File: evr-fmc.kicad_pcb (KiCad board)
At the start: 6 copper layers, 84 x 69 mm, 256 parts, among them J1 MMCX, J10 MMCX, J11 MMCX, J12 MMCX, J13 MMCX, J14 MMCX, J15 MMCX, J16 MMCX, J17 MMCX, J18 MMCX, J19 WP Jumper, J2 MMCX, J20 MMCX, J21 MMCX, J3 MMCX, J4 MMCX, J5 MMCX, J6 MMCX, J7 MMCX, J8 MMCX, J9 MMCX, P1 ASP-134488-01, Q1 FDN335N, Q2 FDN335N, Q3 FDN335N, T1 TCM2-43X+, T2 TCM2-43X+, T3 TCM2-43X+, T4 TCM2-43X+, U1 SN74LVC3G34DCT, U10 SN74LVC3G34DCT, U11 SN74LVC3G34DCT, U12 SN74LVC3G34DCT, U13 SN74LVC3G34DCT, U14 SN74LVC3G34DCT, U15 SN74LVC3G34DCT, U16 SN74LVC3G34DCT, U17 SN74LVC3G34DCT, U18 SI5394, U19 SI5394, U2 SN74LVC3G34DCT, U20 TLV75733PDBV, U21 TLV75718PDBV, U22 TPS562200, U23 74AVC4T245, U24 TLV75733PDBV, U25 74AVC4T245, U26 74LVC8T245, U27 74LVC8T245, U28 TLV75718PDBV, U3 SN74LVC3G34DCT, U4 SN74LVC3G34DCT, U5 SN74LVC3G34DCT, U6 SN74LVC3G34DCT, U7 SN74LVC3G34DCT, U8 SN74LVC3G34DCT, U9 AT24C64D, Y1 CX3225SB48000D0FPJC1, Y2 CX3225SB48000D0FPJC1

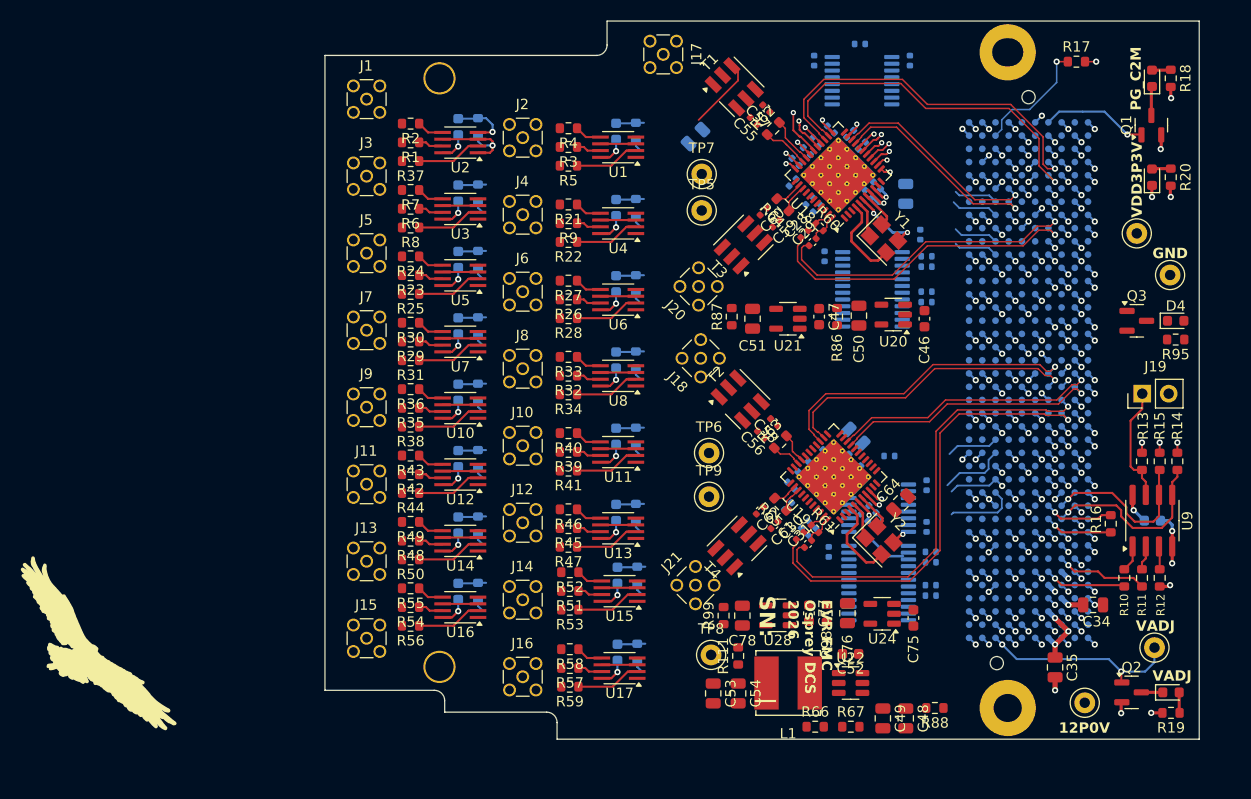
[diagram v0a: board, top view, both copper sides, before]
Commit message: Layout draft nearly complete
- Changed some digital IO pinout on the FMC
- Most areas routed
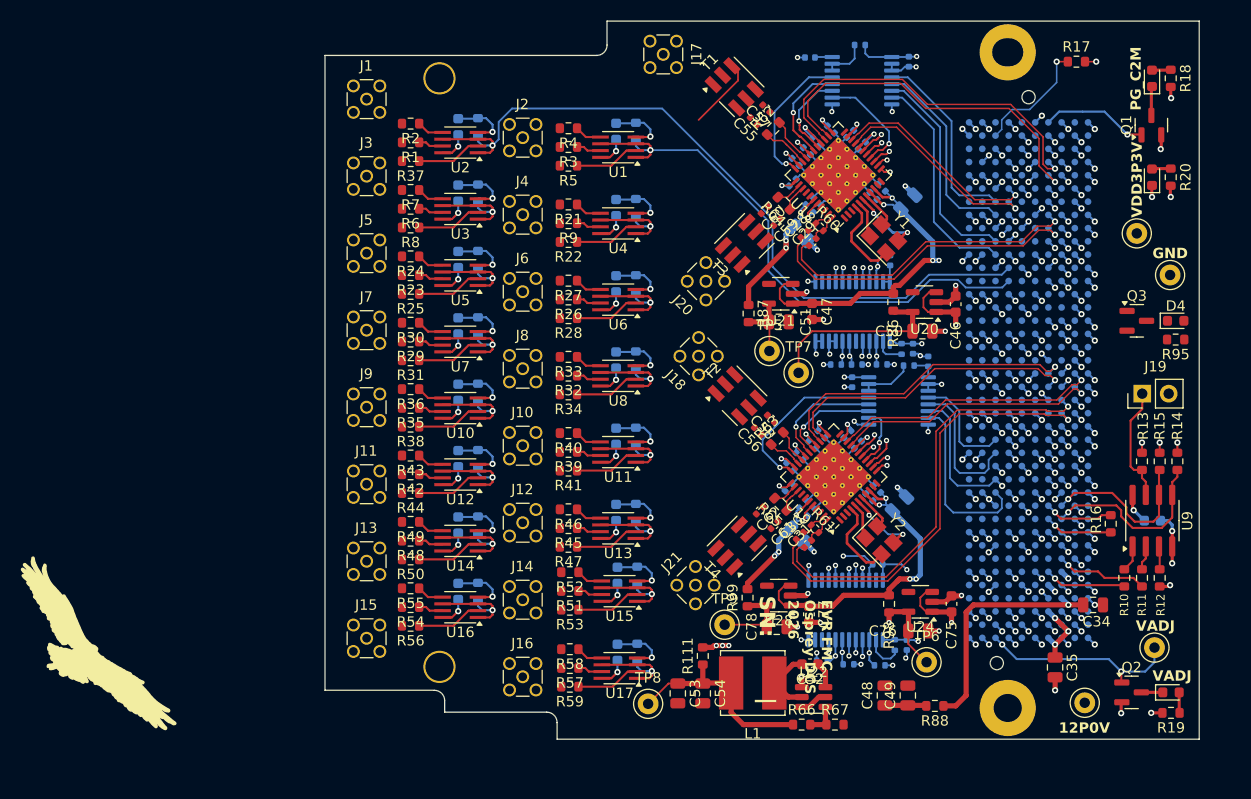
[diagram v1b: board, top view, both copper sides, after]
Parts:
- C64: moved to B.Cu
- moved TP6 29.0 mm to (164.8, 132.6)
- moved TP7 21.2 mm to (152.5, 104.8)
- moved TP5 15.0 mm to (149.7, 102.7)
- moved C73 13.7 mm to (152.7, 91.4), turned to -45 degrees
- moved TP9 12.4 mm to (145.4, 129.0)
- moved R94 12.2 mm to (154.8, 132.4), turned to 0 degrees
- moved C68 11.9 mm to (165.0, 103.7), turned to -90 degrees
- moved C71 11.5 mm to (162.9, 130.9), turned to 90 degrees
- moved R92 11.0 mm to (160.3, 132.9)
- moved C74 11.0 mm to (152.4, 120.4)
- moved C69 11.0 mm to (163.5, 102.5), turned to 90 degrees
- moved R90 11.0 mm to (157.3, 132.8)
- moved R93 10.6 mm to (156.1, 104.0), turned to 0 degrees
- moved C67 10.5 mm to (157.7, 105.7)
- moved U25 10.5 mm to (162.1, 107.5)
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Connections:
- P1 pad C10: /FMC/Cleaner_SPI_0.CS -> /FMC/Cleaner_SPI_0.CLK
- P1 pad C11: /FMC/Cleaner_~{RST}_0 -> /FMC/Cleaner_SPI_0.SDI
- P1 pad D12: /FMC/Cleaner_SPI_0.CLK -> /FMC/Cleaner_SPI_0.OE
- P1 pad D26: /FMC/Cleaner_SPI_1.CS -> /FMC/Cleaner_SPI_1.SDI
- P1 pad D27: /FMC/Cleaner_~{RST}_1 -> /FMC/Cleaner_SPI_1.OE
- P1 pad G10: /FMC/Cleaner_SPI_0.SDI -> /FMC/Cleaner_SPI_0.CS
- P1 pad G24: /FMC/Cleaner_SPI_1.OE -> /FMC/Cleaner_~{RST}_1
- P1 pad G25: /FMC/Cleaner_SPI_1.SDI -> /FMC/Cleaner_SPI_1.CS
- P1 pad G9: /FMC/Cleaner_SPI_0.OE -> /FMC/Cleaner_~{RST}_0
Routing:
- net GND: track 202.6 -> 368.8 mm, vias 167 -> 217
- net /Digital IO/D_Output0: track 9.38 -> 72.9 mm
- net /Digital IO/D_Output1: track 4.54 -> 54.1 mm, vias 0 -> 1
- net Net-(U20-EN): track 0.00 -> 43.0 mm, vias 0 -> 5
- net /FMC/Cleaner_SPI_1.CLK: track 0.91 -> 35.6 mm, vias 1 -> 2
- net /FMC/Cleaner_SPI_1.SDI: track 0.00 -> 34.4 mm, vias 0 -> 2
- net /FMC/Cleaner_~{RST}_1: track 0.91 -> 35.1 mm, vias 1 -> 2
- net /FMC/Cleaner_SPI_1.CS: track 0.91 -> 33.3 mm, vias 1 -> 2
- net P1_VADJ: track 26.3 -> 57.1 mm, vias 6 -> 18
- net /FMC/Cleaner_SPI_1.OE: track 4.01 -> 33.8 mm, vias 0 -> 2
- net /Jitter Cleaner0/VDDA: track 5.67 -> 35.2 mm, vias 2 -> 4
- net /FMC/Cleaner_SPI_0.CLK: track 0.00 -> 29.0 mm, vias 0 -> 2
- net /FMC/Cleaner_SPI_0.SDI: track 0.00 -> 27.6 mm, vias 0 -> 2
- net /Jitter Cleaner1/VDDA: track 5.67 -> 33.1 mm, vias 2 -> 4
- net /FMC/Cleaner_SPI_0.CS: track 0.00 -> 26.1 mm, vias 0 -> 2
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- added copper zone on In3.Cu, net /Jitter Cleaner0/VDD
- added copper zone on In3.Cu, net /Jitter Cleaner1/VDD
- removed copper zone on In2.Cu, net +12V_FMC

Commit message: Draft Layout Complete
-Draft Layout Complete
- Silkscreen need to be complete
- some Digital IO swapped FMC pins
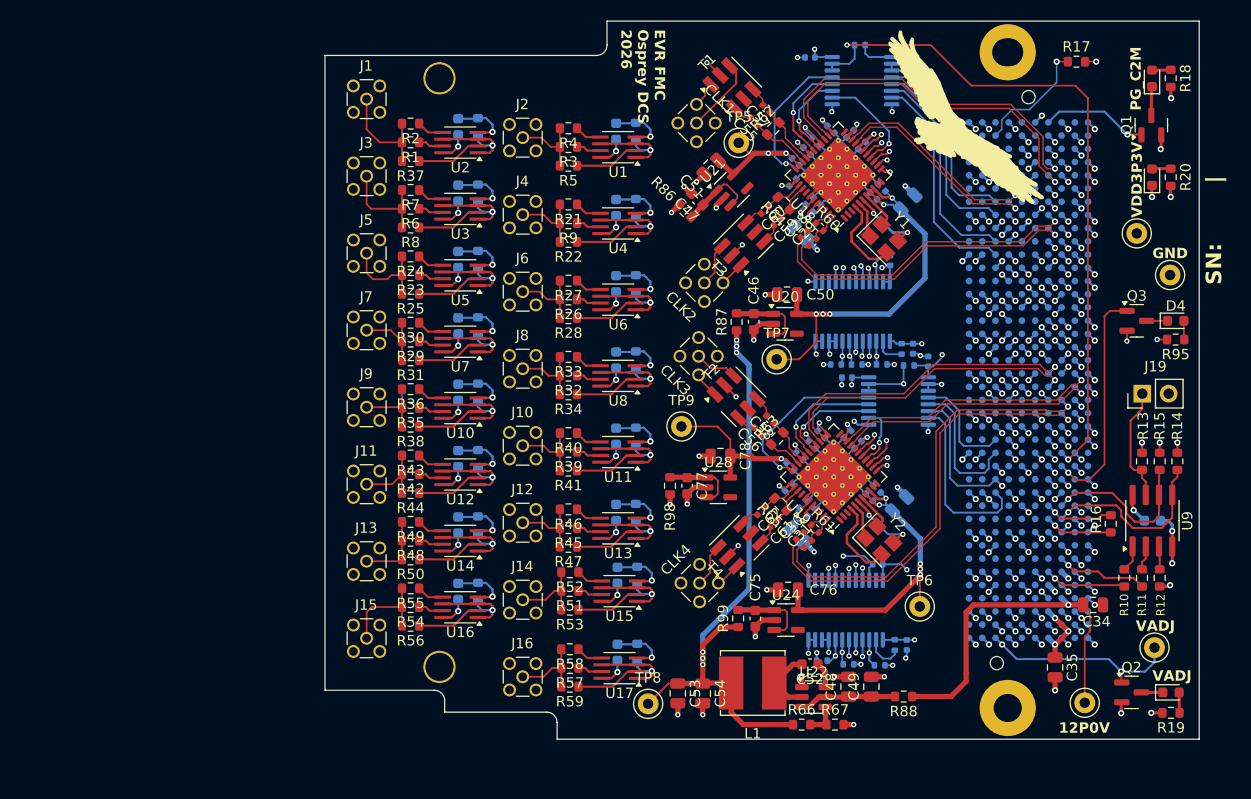
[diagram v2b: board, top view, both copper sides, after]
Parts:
- removed R111: 0R, Resistor_SMD:R_0603_1608Metric
- moved Logo1 97.5 mm to (168.6, 80.9)
- moved R98 23.9 mm to (140.2, 115.7)
- moved R86 21.8 mm to (141.6, 89.3), turned to -45 degrees
- moved TP5 20.2 mm to (146.8, 82.7)
- moved TP9 19.5 mm to (141.2, 110.0)
- moved C46 19.5 mm to (148.2, 99.9), turned to -90 degrees
- moved C75 18.9 mm to (148.3, 128.4), turned to -90 degrees
- moved C78 17.3 mm to (145.0, 112.8), turned to 180 degrees
- moved C77 17.0 mm to (141.8, 115.7)
- moved C51 16.2 mm to (144.1, 85.0), turned to -135 degrees
- moved C47 15.4 mm to (142.8, 88.1), turned to 135 degrees
- moved U20 13.6 mm to (151.2, 100.1), turned to 0 degrees
- moved C50 13.5 mm to (151.4, 97.3), turned to 180 degrees
- moved C76 13.1 mm to (151.5, 125.7), turned to 180 degrees
- moved U24 13.0 mm to (151.3, 128.6), turned to 0 degrees
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- renumbered J17 to CLK1, J20 to CLK2, J18 to CLK3, J21 to CLK4
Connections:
- C47 pad 1: /Jitter Cleaner0/VDDA -> Net-(U21-EN)
- C50 pad 1: Net-(U20-OUT) -> /Jitter Cleaner0/VDDA
- C51 pad 1: Net-(U21-OUT) -> /Jitter Cleaner0/VDD
- C53 pad 1: Net-(C53-Pad1) -> /Jitter Cleaner0/Switched_4P3V
- C54 pad 1: Net-(C53-Pad1) -> /Jitter Cleaner0/Switched_4P3V
- C55 pad 2: Net-(T1-SEC) -> Net-(T1-SEC_DOT)
- C56 pad 2: Net-(T2-SEC) -> Net-(T2-SEC_DOT)
- C57 pad 2: Net-(T1-SEC_DOT) -> Net-(T1-SEC)
- C58 pad 2: Net-(T2-SEC_DOT) -> Net-(T2-SEC)
- C59 pad 2: Net-(T3-SEC) -> Net-(T3-SEC_DOT)
- C60 pad 2: Net-(T3-SEC_DOT) -> Net-(T3-SEC)
- C61 pad 2: Net-(T4-SEC) -> Net-(T4-SEC_DOT)
- C62 pad 2: Net-(T4-SEC_DOT) -> Net-(T4-SEC)
- C75 pad 1: Net-(U20-EN) -> Net-(U24-EN)
- C76 pad 1: Net-(U24-OUT) -> /Jitter Cleaner1/VDDA
- C77 pad 1: /Jitter Cleaner1/VDDA -> Net-(U28-EN)
- C78 pad 1: Net-(U28-OUT) -> /Jitter Cleaner1/VDD
- L1 pad 2: Net-(C53-Pad1) -> /Jitter Cleaner0/Switched_4P3V
- P1 pad C14: /Digital IO/D_Output4 -> /Digital IO/D_Output6
- P1 pad C15: /Digital IO/D_Output5 -> /Digital IO/D_Output7
- P1 pad C18: /Digital IO/D_Output10 -> /Digital IO/D_Output14
- P1 pad C19: /Digital IO/D_Output11 -> /Digital IO/D_Output15
- P1 pad D17: /Digital IO/D_Output8 -> /Digital IO/D_Output10
- P1 pad D18: /Digital IO/D_Output9 -> /Digital IO/D_Output11
- P1 pad G15: /Digital IO/D_Output6 -> /Digital IO/D_Output4
- P1 pad G16: /Digital IO/D_Output7 -> /Digital IO/D_Output5
- P1 pad G18: /Digital IO/D_Output12 -> /Digital IO/D_Output8
- P1 pad G19: /Digital IO/D_Output13 -> /Digital IO/D_Output9
- P1 pad G21: /Digital IO/D_Output14 -> /Digital IO/D_Output12
- P1 pad G22: /Digital IO/D_Output15 -> /Digital IO/D_Output13
- R66 pad 1: Net-(C53-Pad1) -> /Jitter Cleaner0/Switched_4P3V
- R86 pad 1: Net-(U20-OUT) -> VDD3P3V
- R86 pad 2: /Jitter Cleaner0/VDDA -> Net-(U21-EN)
- R87 pad 1: Net-(U21-OUT) -> /Jitter Cleaner0/Switched_4P3V
- R87 pad 2: /Jitter Cleaner0/VDD -> Net-(U20-EN)
- R96 pad 1: /Jitter Cleaner0/OE_Faults -> /FMC/Cleaner_~{OE}_0
- R97 pad 1: /Jitter Cleaner1/OE_Faults -> /FMC/Cleaner_~{OE}_1
- R98 pad 1: Net-(U24-OUT) -> VDD3P3V
- R98 pad 2: /Jitter Cleaner1/VDDA -> Net-(U28-EN)
- R99 pad 1: Net-(U28-OUT) -> /Jitter Cleaner0/Switched_4P3V
- R99 pad 2: /Jitter Cleaner1/VDD -> Net-(U24-EN)
- TP5 pad 1: Net-(U21-OUT) -> /Jitter Cleaner0/VDD
- TP6 pad 1: Net-(U24-OUT) -> /Jitter Cleaner1/VDDA
- TP7 pad 1: Net-(U20-OUT) -> /Jitter Cleaner0/VDDA
- TP8 pad 1: Net-(C53-Pad1) -> /Jitter Cleaner0/Switched_4P3V
- TP9 pad 1: Net-(U28-OUT) -> /Jitter Cleaner1/VDD
- U20 pad 5: Net-(U20-OUT) -> /Jitter Cleaner0/VDDA
- U21 pad 1: /Jitter Cleaner0/VDDA -> Net-(U21-EN)
- U21 pad 3: /Jitter Cleaner0/VDDA -> Net-(U21-EN)
- U21 pad 5: Net-(U21-OUT) -> /Jitter Cleaner0/VDD
- U23 pad 14: /Jitter Cleaner0/OE_Faults -> /FMC/Cleaner_~{OE}_0
- U23 pad 15: /Jitter Cleaner0/OE_Faults -> /FMC/Cleaner_~{OE}_0
- U24 pad 1: Net-(U20-EN) -> Net-(U24-EN)
- U24 pad 3: Net-(U20-EN) -> Net-(U24-EN)
- U24 pad 5: Net-(U24-OUT) -> /Jitter Cleaner1/VDDA
- U25 pad 14: /Jitter Cleaner1/OE_Faults -> /FMC/Cleaner_~{OE}_1
- U25 pad 15: /Jitter Cleaner1/OE_Faults -> /FMC/Cleaner_~{OE}_1
- U28 pad 1: /Jitter Cleaner1/VDDA -> Net-(U28-EN)
- U28 pad 3: /Jitter Cleaner1/VDDA -> Net-(U28-EN)
- U28 pad 5: Net-(U28-OUT) -> /Jitter Cleaner1/VDD
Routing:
- net /Digital IO/D_Output14: track 9.38 -> 83.5 mm, vias 1 -> 2
- net /FMC/Cleaner_~{OE}_0: track 0.00 -> 66.7 mm, vias 0 -> 2
- net /Digital IO/D_Output15: track 9.38 -> 71.4 mm, vias 1 -> 2
- net /Digital IO/D_Output10: track 9.38 -> 70.5 mm, vias 1 -> 2
- net /Jitter Cleaner0/Switched_4P3V: track 0.00 -> 60.3 mm, vias 0 -> 6
- net /Digital IO/D_Output2: track 9.38 -> 69.5 mm, vias 1 -> 2
- net /Digital IO/D_Output12: track 9.38 -> 68.3 mm, vias 1 -> 2
- net /Digital IO/D_Output6: track 9.38 -> 66.1 mm, vias 1 -> 2
- net /Digital IO/D_Output8: track 9.38 -> 63.8 mm, vias 1 -> 2
- net /Digital IO/D_Output4: track 9.38 -> 63.0 mm, vias 1 -> 2
- net /Digital IO/D_Output11: track 9.38 -> 58.3 mm, vias 1 -> 2
- net /Digital IO/D_Output13: track 9.38 -> 56.1 mm, vias 1 -> 2
- net /Digital IO/D_Output7: track 9.38 -> 52.6 mm, vias 1 -> 2
- net /Digital IO/D_Output3: track 9.38 -> 51.2 mm, vias 1 -> 2
- net /Digital IO/D_Output9: track 9.38 -> 49.4 mm, vias 1 -> 2
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- removed copper zone on In3.Cu, net /Jitter Cleaner0/VDD
- removed copper zone on In3.Cu, net /Jitter Cleaner1/VDD
- removed copper zone on In2.Cu, net P1_3P3VAUX

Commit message: Final Draft - Ready to Review
Things to do:
Round diff traces before generting fabrication files
Change name of project to 'trigger output fmc'
Align this with recent updates to fmc-template

Updates:
- Cleaned up BOM
- Arranged silkscreen and fab layers
- Shortened power traces from LDOs to Jitter Cleaner IC
- Fixed traces/planes with sharp corners
- Straightened out all MMCX Test Ports
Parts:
- moved Logo1 21.3 mm to (173.3, 101.7)
- moved CLK1 6.42 mm to (143.2, 74.4)
- moved R98 4.56 mm to (144.0, 118.1), turned to 135 degrees
- moved TP5 4.05 mm to (142.8, 81.8)
- moved C77 3.60 mm to (145.2, 116.9), turned to -45 degrees
- moved U28 2.75 mm to (147.4, 114.9), turned to 45 degrees
- moved C55 1.20 mm to (149.1, 81.5)
- moved R62 1.20 mm to (150.9, 82.2)
- moved T1 1.20 mm to (146.9, 78.2)
- moved C57 1.20 mm to (150.2, 80.2)
- moved C78 0.45 mm to (145.4, 112.6), turned to -135 degrees
- moved C27 0.25 mm to (154.4, 82.4)
- moved C66 0.20 mm to (163.3, 74.9)
- moved C21 0.14 mm to (153.4, 83.4)
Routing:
- net VDD3P3V: track 79.1 -> 83.2 mm
- net Net-(CLK1-In): track 7.33 -> 4.25 mm
- net /Jitter Cleaner1/VDDA: track 34.8 -> 36.4 mm
- net /Jitter Cleaner0/INTR: track 13.7 -> 15.2 mm
- net GND: track 400.6 -> 402.1 mm
- net /Jitter Cleaner0/VDDA: track 39.4 -> 40.7 mm
- net /Jitter Cleaner0/Cleaned_CLK2.N: track 5.91 -> 4.71 mm
- net /Jitter Cleaner0/Cleaned_CLK2.P: track 5.89 -> 4.69 mm
- net /Jitter Cleaner0/LOL: track 8.32 -> 9.52 mm
- net /Jitter Cleaner0/Switched_4P3V: track 60.3 -> 61.5 mm
- net /FMC/Cleaner_Fault_1.LOL: track 13.9 -> 13.0 mm, vias 1 -> 0
- net /Jitter Cleaner0/LOS_XO: track 9.91 -> 10.8 mm
- net /Digital IO/D_Output12: track 68.3 -> 69.2 mm
- net /Jitter Cleaner1/VDD: track 41.0 -> 41.7 mm, vias 4 -> 5
- net /Digital IO/D_Output11: track 58.3 -> 59.0 mm
